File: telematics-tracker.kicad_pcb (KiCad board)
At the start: 4 copper layers, 82 x 62 mm, 216 parts, among them J1 WAFER-MX3.0-12PZZ, J2 B3B-XH-A, Q1 AM2390N-TP, Q10 MMBT3904, Q11 MMBT3904, Q12 MMBT3904, Q13 MMBT3906, Q14 MMBT3904, Q2 AM2390N-TP, Q3 AO3401A, Q4 MMBT3904, Q5 MMBT3904, Q6 MMBT3904, Q7 MMBT3904, Q8 MMBT3904, Q9 MMBT3904, U1 EC200UCNAA-N05-SGNSA, U2 AT32F403ACGT7, U3 QMI8658B, U4 SIT1051AT/3, U5 EG11752, U6 BQ25606RGER, U7 GD25Q64ESIGR, U8 TXB0104PWR, U9 ME6211C33M5G, X1 NANO-SIM, X2 MFF2-eSIM-pads, Y1 8MHz, Y2 32.768kHz

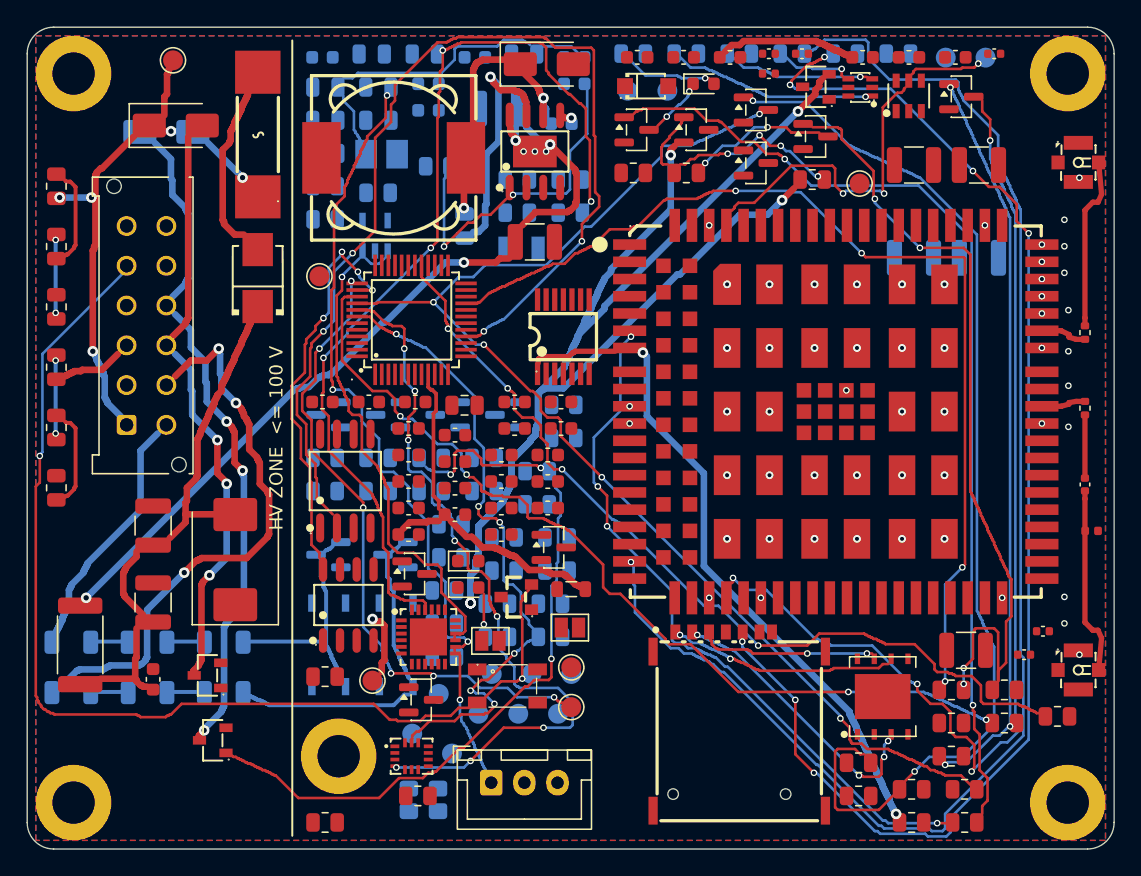
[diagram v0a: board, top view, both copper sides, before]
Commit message: LV routing progress: 25/112 nets (22%)
Co-Authored-By: Claude Opus 5 (1M context) <noreply@anthropic.com>
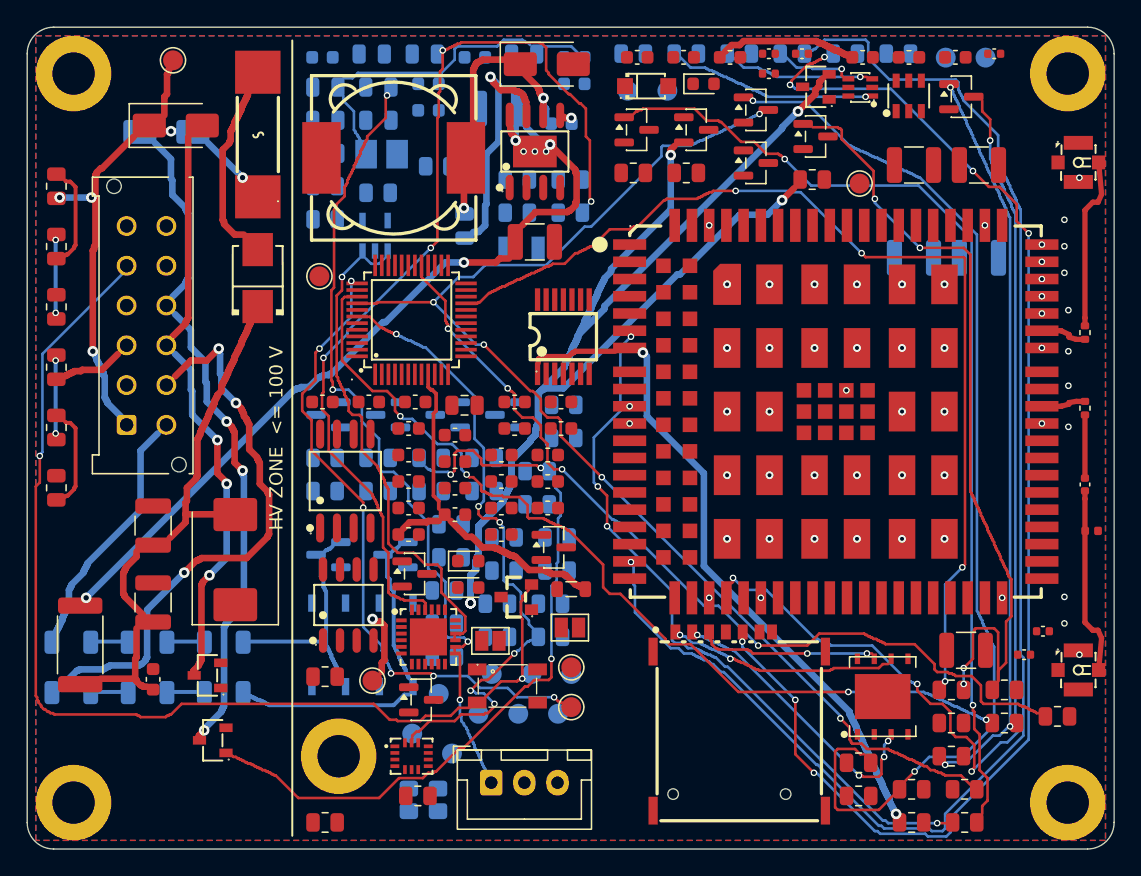
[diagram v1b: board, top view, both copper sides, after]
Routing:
- net SPI1_MISO: track 79.6 -> 0.00 mm, vias 4 -> 0
- net /mcu/IMU_INT1: track 56.6 -> 0.00 mm, vias 8 -> 0
- net CAN_STB: track 29.8 -> 0.00 mm, vias 4 -> 0
- net /modem_rf/USB_VBUS: track 29.1 -> 0.00 mm, vias 3 -> 0
- net /power/U5_VCC: track 24.2 -> 0.00 mm, vias 2 -> 0
- net /modem_rf/Q13_B: track 17.0 -> 0.00 mm, vias 4 -> 0
- net /modem_rf/Q14_C: track 10.0 -> 0.00 mm, vias 2 -> 0
- net /modem_rf/NETLED_A: track 6.86 -> 0.00 mm, vias 1 -> 0
- net /modem_rf/NETLED_K: track 3.79 -> 0.00 mm, vias 2 -> 0
- net /mcu/NSL_A: track 2.60 -> 0.00 mm, vias 1 -> 0

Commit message: adopt: net harvest was a broken state machine, collected zero nets
Co-Authored-By: Claude Opus 5 (1M context) <noreply@anthropic.com>
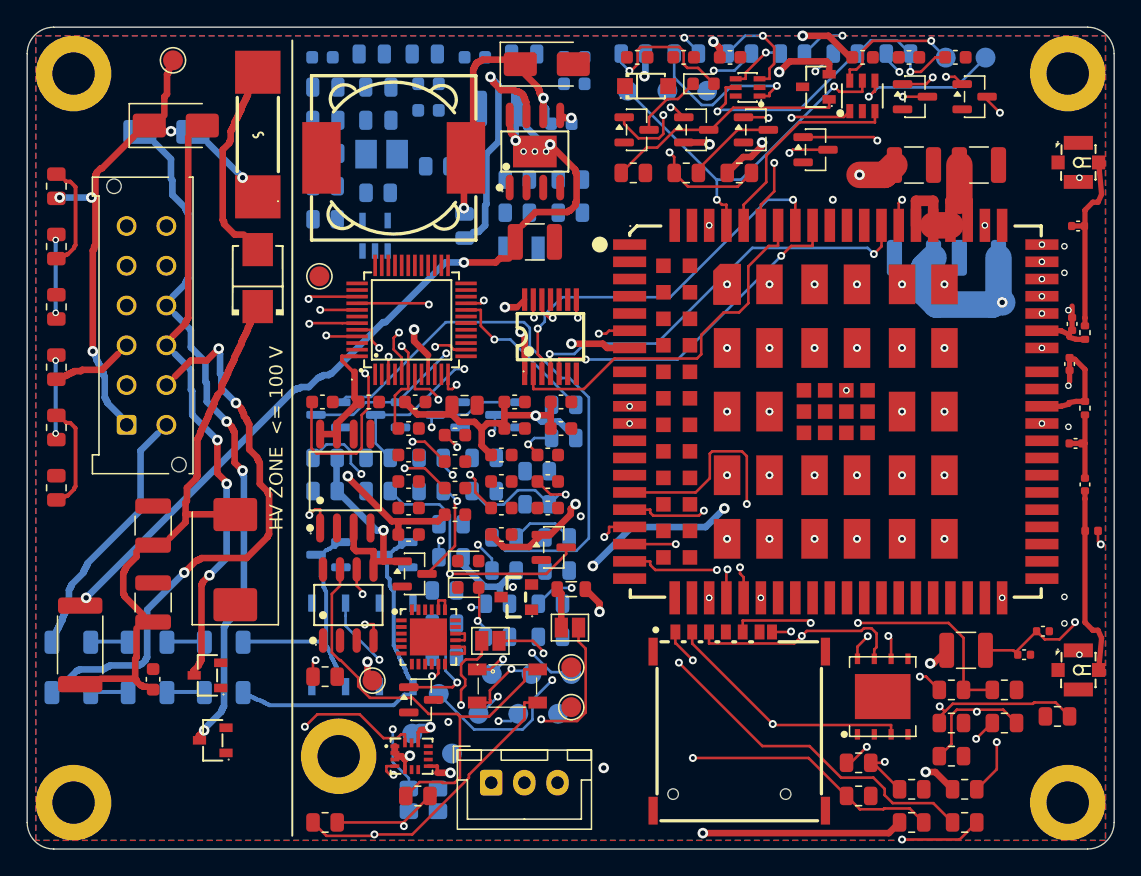
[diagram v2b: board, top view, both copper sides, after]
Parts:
- TP15: moved to B.Cu
- moved C51 36.2 mm to (79.1, 31.4)
- moved C48 30.6 mm to (78.8, 22.4), turned to 90 degrees
- moved TP17 27.1 mm to (45.3, 4.80)
- moved C49 24.5 mm to (79.3, 15.0)
- moved C50 24.1 mm to (78.6, 25.4), turned to -90 degrees
- moved Q11 16.5 mm to (71.5, 5.25)
- moved TP15 11.5 mm to (69.3, 2.30), turned to 180 degrees
- moved D14 8.50 mm to (54.4, 4.54)
- moved R52 5.52 mm to (53.7, 11.0)
- moved Q9 4.61 mm to (59.5, 9.24)
- moved Q14 4.53 mm to (55.0, 7.75)
- moved Q10 3.50 mm to (67.0, 5.25)
- moved D15 3.50 mm to (63.0, 5.19)
- moved TP16 3.00 mm to (72.3, 2.30)
- moved TP18 3.00 mm to (48.3, 4.80)
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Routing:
- net 3V3: track 0.00 -> 154.5 mm, vias 0 -> 11
- net SYS: track 139.8 -> 62.6 mm, vias 7 -> 6
- net /io/CANL: track 79.8 -> 5.91 mm, vias 2 -> 1
- net /power/REGN: track 71.6 -> 0.00 mm, vias 4 -> 0
- net MODEM_PWRKEY: track 65.3 -> 0.00 mm, vias 4 -> 0
- net /modem_rf/Q9_B: track 0.00 -> 62.1 mm, vias 0 -> 2
- net /modem_rf/USIM_VDD: track 0.00 -> 61.3 mm, vias 0 -> 3
- net /modem_rf/U8_OE: track 0.00 -> 59.0 mm, vias 0 -> 2
- net /mcu/BOOT0: track 0.00 -> 58.8 mm, vias 0 -> 3
- net /power/VBAT_BT: track 60.0 -> 1.90 mm, vias 4 -> 0
- net /power/SYS: track 59.9 -> 1.90 mm, vias 1 -> 0
- net /io/Q2_G: track 56.0 -> 0.00 mm, vias 3 -> 0
- net /modem_rf/VDD_EXT_1V8: track 59.0 -> 113.3 mm, vias 2 -> 5
- net /modem_rf/USIM_RST_M: track 108.6 -> 54.7 mm, vias 1 -> 2
- net /modem_rf/USIM_VDD_SIM: track 99.6 -> 50.2 mm, vias 7 -> 2
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
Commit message: Shunt rotations: pad 1 faces the line; name-based net rip for KiCad 10
KiCad 10 references nets by NAME on every item - (net "GND") - not through
a numeric table; the ripper matched nothing until rewritten. And all four
pi-shunt orientations were backwards: each T-stub crossed its own GND pad
(6 shorts + 6 mask bridges, measured, now impossible by construction).

Co-Authored-By: Claude Opus 5 (1M context) <noreply@anthropic.com>
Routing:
- net /modem_rf/VDD_EXT_1V8: track 113.3 -> 0.00 mm, vias 5 -> 0
- net /modem_rf/SIM_CLK: track 76.5 -> 0.00 mm, vias 3 -> 0
- net /modem_rf/Q12_B: track 75.0 -> 0.00 mm, vias 2 -> 0
- net /modem_rf/USIM_RST_M: track 54.7 -> 0.00 mm, vias 2 -> 0
- net /modem_rf/USIM_DATA_M: track 44.3 -> 0.00 mm, vias 2 -> 0
- net /modem_rf/USIM_DET: track 27.4 -> 0.00 mm, vias 2 -> 0
- net /modem_rf/ANT_GNSS_M: track 9.09 -> 5.20 mm
- net /io/DI2_LED: track 26.6 -> 23.2 mm
- net /io/DI1_LED: track 19.0 -> 16.3 mm

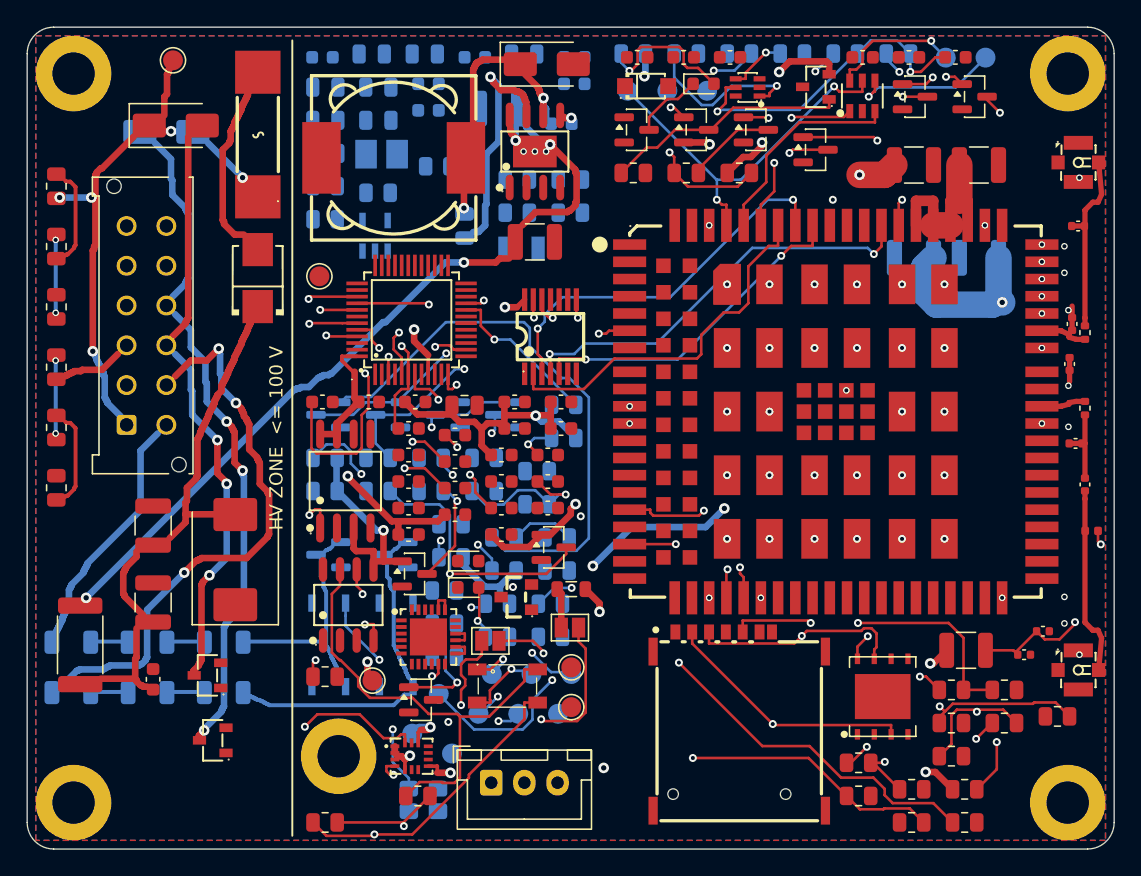
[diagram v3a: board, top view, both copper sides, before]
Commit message: Shunts outboard of the corner elbows; iterative adopt rip
C48/C50 between the runs landed in the mitred-corner elbow and their GND
pads fouled the diagonal at 0.04..0.22 mm (6 locked-copper violations).
They now sit on the outer side of their runs; the fence via beneath each is
auto-suppressed - an accepted local fence gap at a DNP option position.

adopt now iterates rip->refill->DRC up to 3x on the ADOPTED board: some
violations only manifest post-refill, and FreeRouting cannot know the 1.5mm
HV rule (a DSN carries netclass values only) - measured: it routed SYS_LED
1.27 mm from locked VIN_B inside the strip. Ripped nets reroute under the
LV finisher's full rule model. Violations on locked copper = hard fail.

Co-Authored-By: Claude Opus 5 (1M context) <noreply@anthropic.com>
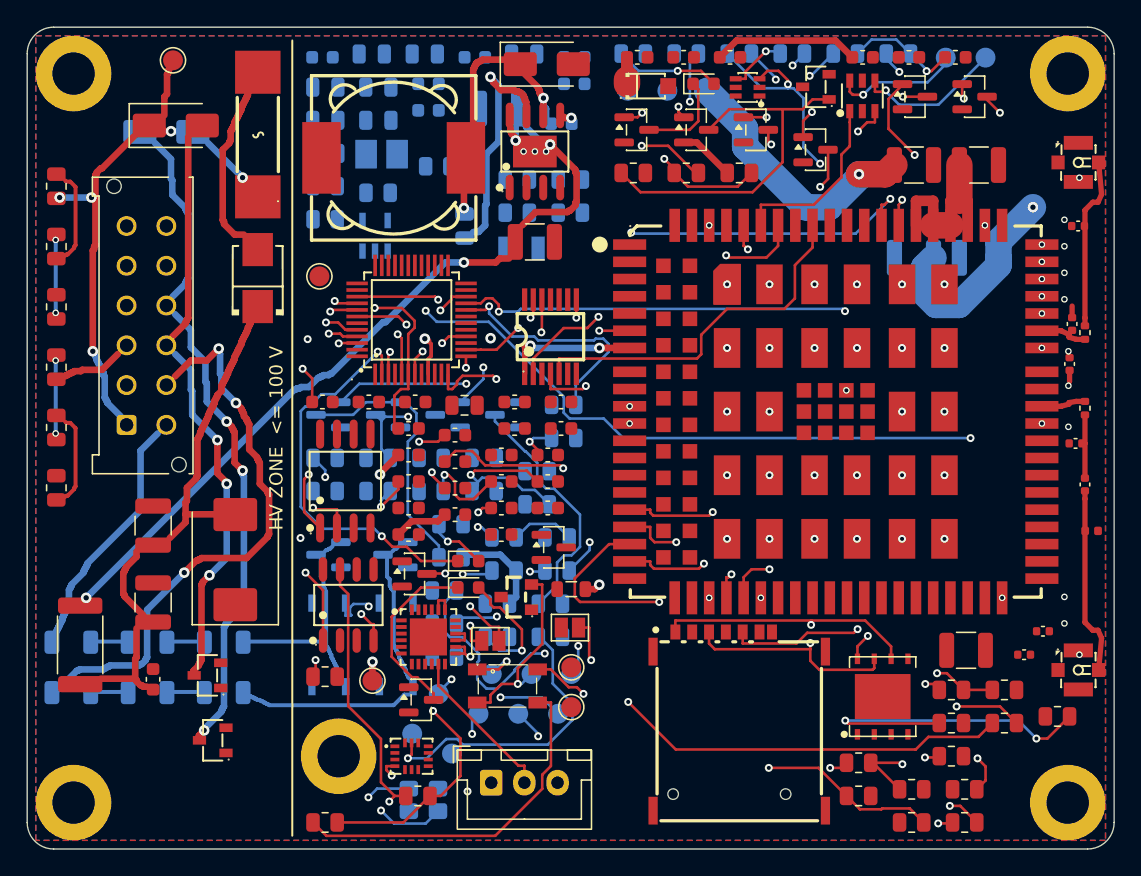
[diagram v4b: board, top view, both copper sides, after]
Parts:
- turned C48 to -90 degrees
- turned C49 to 180 degrees
- turned C50 to 90 degrees
- turned C51 to 180 degrees
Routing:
- net 3V3: track 154.5 -> 0.00 mm, vias 11 -> 0
- net /modem_rf/SIM_DATA: track 84.1 -> 0.00 mm, vias 2 -> 0
- net /modem_rf/SIM_CLK: track 0.00 -> 70.8 mm, vias 0 -> 3
- net /modem_rf/Q12_B: track 0.00 -> 67.3 mm, vias 0 -> 2
- net /mcu/I2C1_SCL: track 0.00 -> 66.5 mm, vias 0 -> 2
- net SYS: track 62.6 -> 5.65 mm, vias 6 -> 1
- net /modem_rf/USIM_RST_M: track 0.00 -> 48.6 mm, vias 0 -> 2
- net /mcu/I2C1_SDA: track 43.8 -> 0.00 mm, vias 2 -> 0
- net /modem_rf/USIM_DATA_M: track 0.00 -> 42.0 mm, vias 0 -> 2
- net /mcu/OSC_IN: track 22.0 -> 59.2 mm, vias 2 -> 4
- net /mcu/DBG_RX: track 0.00 -> 32.6 mm, vias 0 -> 2
- net /mcu/NET_STATUS_LED: track 0.00 -> 32.2 mm, vias 0 -> 2
- net /mcu/SYS_LED: track 0.00 -> 30.3 mm, vias 0 -> 2
- net /modem_rf/MTXD_1V8: track 29.1 -> 0.00 mm, vias 2 -> 0
- net /modem_rf/USB_VBUS: track 28.4 -> 0.00 mm, vias 2 -> 0
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
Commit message: Pin pi shunts clear of the corner elbows (FIXED set)
Co-Authored-By: Claude Opus 5 (1M context) <noreply@anthropic.com>
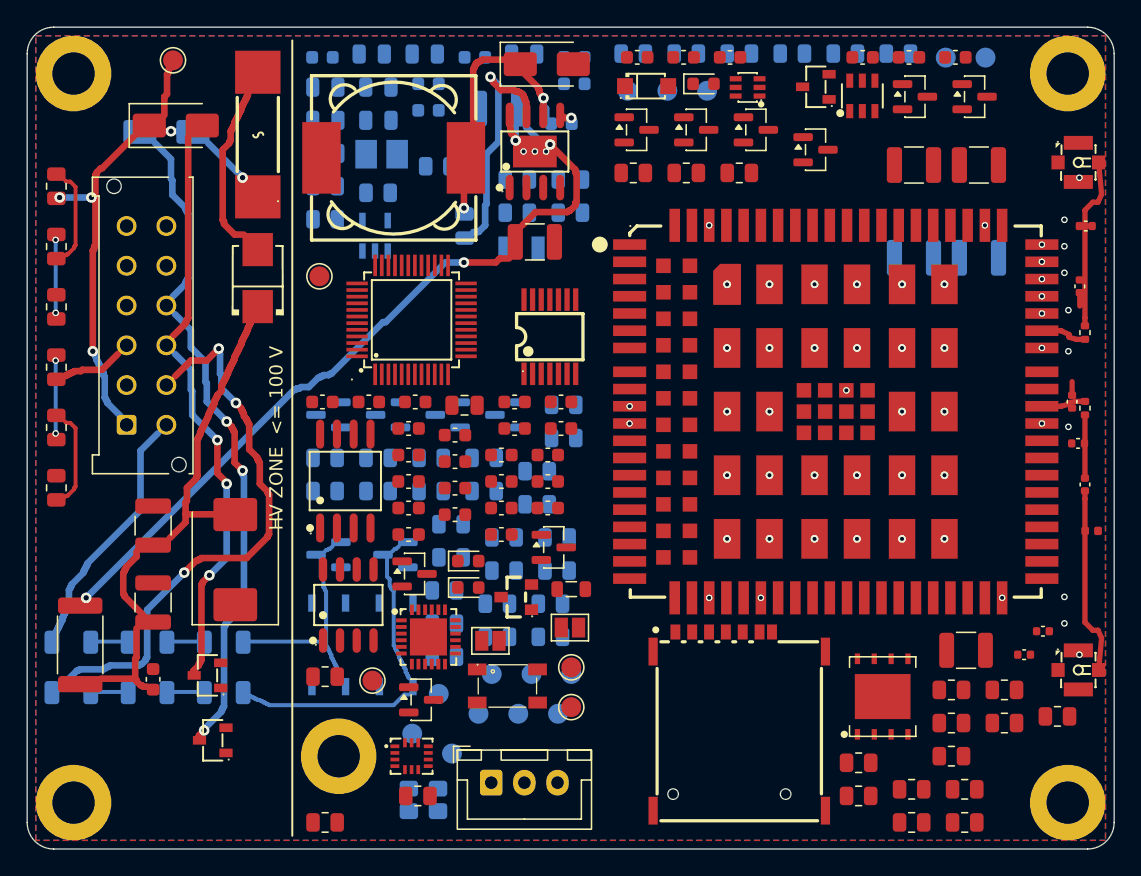
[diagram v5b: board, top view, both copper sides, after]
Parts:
- moved C48 2.90 mm to (79.4, 19.6), turned to 90 degrees
- moved C50 2.85 mm to (78.8, 28.2), turned to -90 degrees
- moved C49 0.58 mm to (79.9, 15.0)
- moved C51 0.19 mm to (79.3, 31.4)
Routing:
- net MODEM_STATUS: track 109.2 -> 0.00 mm, vias 5 -> 0
- net MODEM_RESET: track 76.2 -> 0.00 mm, vias 2 -> 0
- net /modem_rf/Q9_B: track 74.5 -> 0.00 mm, vias 3 -> 0
- net /mcu/BOOT0: track 71.7 -> 0.00 mm, vias 3 -> 0
- net /modem_rf/SIM_CLK: track 70.8 -> 0.00 mm, vias 3 -> 0
- net /modem_rf/Q12_B: track 67.3 -> 0.00 mm, vias 2 -> 0
- net /modem_rf/SIM_RST: track 66.6 -> 0.00 mm, vias 2 -> 0
- net /mcu/I2C1_SCL: track 66.5 -> 0.00 mm, vias 2 -> 0
- net /mcu/OSC_OUT: track 65.7 -> 0.00 mm, vias 3 -> 0
- net /modem_rf/USIM_VDD: track 63.9 -> 0.00 mm, vias 2 -> 0
- net /modem_rf/Q14_B: track 63.2 -> 0.00 mm, vias 2 -> 0
- net MODEM_PWR_EN: track 61.5 -> 0.00 mm, vias 3 -> 0
- net /modem_rf/Q10_B: track 60.9 -> 0.00 mm, vias 3 -> 0
- net /modem_rf/USIM_CLK_M: track 60.2 -> 0.00 mm, vias 2 -> 0
- net /mcu/OSC_IN: track 59.2 -> 0.00 mm, vias 4 -> 0
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
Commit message: F-24: module-side pi shunts to B.Cu with tap vias; connector-side at x=79.0
Measured exhaustively on F.Cu for C48/C50: between the runs they foul the
mitre elbow (6 violations), outboard they foul the fence rows (14), and
U1's outer NC-pad ring reaches x=77.65, leaving no legal 0402 column. They
sit on B.Cu under the corridor with one tap via each onto their run's
vertical - a documented compromise on DNP OPTION pads, flagged F-24: if pi
matching is ever actually needed, the recommended path is a corridor-width
respin. C49/C51 stay top-side at x=79.0 (pad 2 clears the NC ring by 0.87).
Pre-autoroute DRC: 0 error violations, RF ratsnest closed.

Co-Authored-By: Claude Opus 5 (1M context) <noreply@anthropic.com>
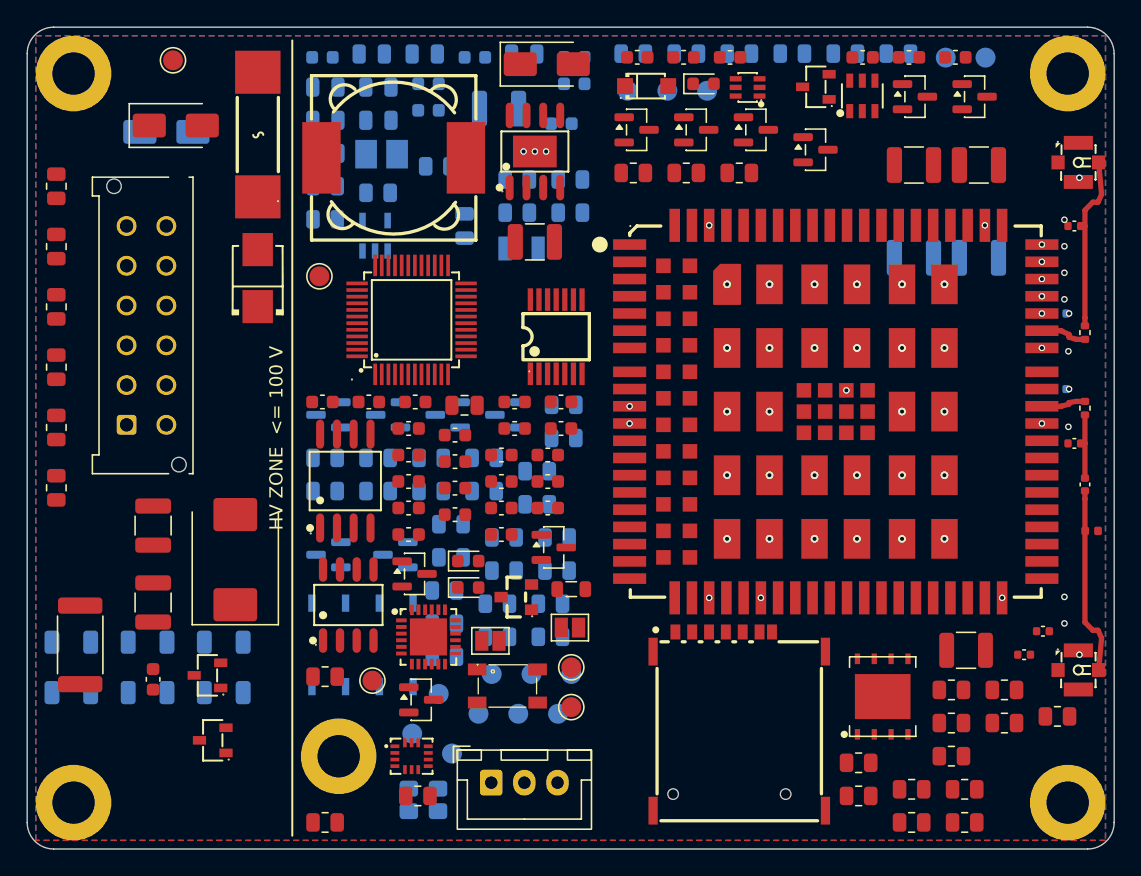
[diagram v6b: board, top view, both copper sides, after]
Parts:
- C48, C50: moved to B.Cu
- moved C48 2.55 mm to (77.9, 21.6), turned to 180 degrees
- moved C50 1.33 mm to (77.9, 27.3), turned to 180 degrees
- moved C49 0.86 mm to (79.0, 15.0)
- moved U8 0.48 mm to (39.9, 23.4)
- moved C51 0.28 mm to (79.0, 31.4)
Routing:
- net /power/VIN_B: track 57.5 -> 0.00 mm, vias 7 -> 3
- net /io/DO2_OUT: track 48.6 -> 0.00 mm, vias 3 -> 0
- net /io/DI2_IN: track 42.7 -> 0.00 mm, vias 3 -> 0
- net /io/DO1_OUT: track 42.2 -> 0.00 mm, vias 3 -> 0
- net /power/VIN_P: track 34.6 -> 0.00 mm
- net VIN: track 34.4 -> 0.00 mm, vias 5 -> 0
- net /io/DI2_LED: track 23.2 -> 0.00 mm
- net /io/DI1_IN: track 18.2 -> 0.00 mm
- net /power/U5_IS: track 16.8 -> 0.00 mm, vias 1 -> 0
- net /io/DI1_LED: track 16.3 -> 0.00 mm
- net /power/SW_BUCK: track 12.9 -> 0.00 mm, vias 2 -> 0
- net /power/VIN_F: track 12.7 -> 0.00 mm
- net /io/IGN_D1: track 6.60 -> 0.00 mm
- net /io/VIN_D0: track 6.60 -> 0.00 mm
- net /io/VIN_D1: track 5.50 -> 0.00 mm, vias 2 -> 0
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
